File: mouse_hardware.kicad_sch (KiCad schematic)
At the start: 48 parts, among them IC1 ADP150AUJZ-2.0-R7, IC2 AP2112K-3.3TRG1, J1 Conn_01x04_Pin, J2 Conn_01x04_Pin, SW1 SW_Push, SW5 SW_Push, U1 STM32F103RETx, U2 PMW3360DM-T2QU, Y1 8MHz

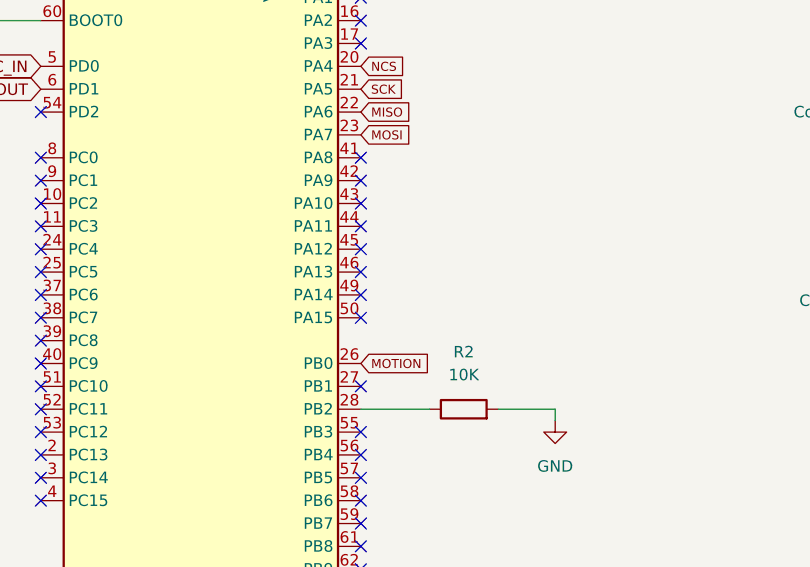
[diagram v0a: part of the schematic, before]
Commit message: Connect SCLK and SWDIO
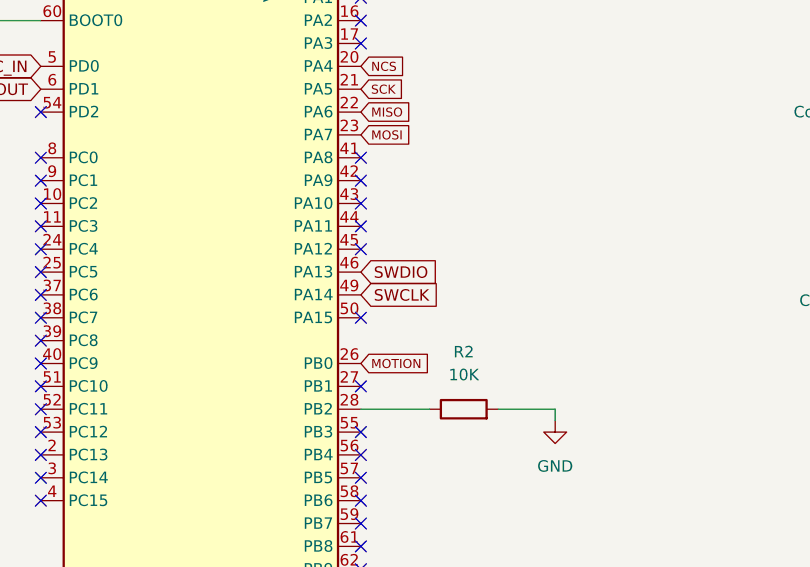
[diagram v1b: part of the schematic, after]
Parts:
- H1, H2, H3: footprint (none) -> Hole:Hole_1.8mm_1.2mm
- J1, J2: footprint Connector_PinHeader_2.54mm:PinHeader_1x04_P2.54mm_Horizontal -> PinHeader:PinHeader_1x04_P2.54mm_Horizontal
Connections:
- net SWCLK: now also U1.49 (PA14)
- net SWDIO: now also U1.46 (PA13)
- no-connect marks 41 -> 39
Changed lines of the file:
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@@
   (no_connect (at 227.33 127))
   (no_connect (at 227.33 200.66))
-  (no_connect (at 227.33 160.02))
   (no_connect (at 227.33 205.74))
   (no_connect (at 227.33 175.26))
@@
   (no_connect (at 191.77 147.32))
   (no_connect (at 80.01 54.61))
-  (no_connect (at 227.33 157.48))
   (no_connect (at 227.33 177.8))
   (no_connect (at 191.77 182.88))
@@
     )
   )
+  (global_label "SWCLK" (shape input) (at 227.33 160.02 0) (fields_autoplaced)
+    (effects (font (size 1.27 1.27)) (justify left))
+    (property "Intersheetrefs" "${INTERSHEET_REFS}" (at 236.5442 160.02 0)
+      (effects (font (size 1.27 1.27)) (justify left) hide)
+    )
+  )
   (global_label "USBDP" (shape input) (at 228.6 198.12 0) (fields_autoplaced)
     (effects (font (size 1 1)) (justify left))
@@
     )
   )
+  (global_label "SWDIO" (shape input) (at 227.33 157.48 0) (fields_autoplaced)
+    (effects (font (size 1.27 1.27)) (justify left))
+    (property "Intersheetrefs" "${INTERSHEET_REFS}" (at 236.1814 157.48 0)
+      (effects (font (size 1.27 1.27)) (justify left) hide)
+    )
+  )
   (global_label "OSC_OUT" (shape input) (at 191.77 137.16 180) (fields_autoplaced)
     (effects (font (size 1.27 1.27)) (justify right))
@@
       (effects (font (size 1.27 1.27)) (justify left))
     )
-    (property "Footprint" "" (at 44.45 180.34 0)
+    (property "Footprint" "Hole:Hole_1.8mm_1.2mm" (at 44.45 180.34 0)
       (effects (font (size 1.27 1.27)) hide)
     )
@@
       (effects (font (size 1.27 1.27)) (justify left))
     )
-    (property "Footprint" "" (at 41.91 214.63 0)
+    (property "Footprint" "Hole:Hole_1.8mm_1.2mm" (at 41.91 214.63 0)
       (effects (font (size 1.27 1.27)) hide)
     )
@@
       (effects (font (size 1.27 1.27)) (justify left))
     )
-    (property "Footprint" "" (at 41.275 251.46 0)
+    (property "Footprint" "Hole:Hole_1.8mm_1.2mm" (at 41.275 251.46 0)
       (effects (font (size 1.27 1.27)) hide)
     )
@@
       (effects (font (size 1.27 1.27)))
     )
-    (property "Footprint" "Connector_PinHeader_2.54mm:PinHeader_1x04_P2.54mm_Horizontal" (at 282.575 165.735 0)
+    (property "Footprint" "PinHeader:PinHeader_1x04_P2.54mm_Horizontal" (at 282.575 165.735 0)
       (effects (font (size 1.27 1.27)) hide)
     )
@@
       (effects (font (size 1.27 1.27)))
     )
-    (property "Footprint" "Connector_PinHeader_2.54mm:PinHeader_1x04_P2.54mm_Horizontal" (at 281.94 144.78 0)
-      (effects (font (size 1.27 1.27)) hide)
-    )
+    (property "Footprint" "PinHeader:PinHeader_1x04_P2.54mm_Horizontal" (at 281.94 144.78 0)
+      (effects (font (size 1.27 1.27)) hide)
+    )

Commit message: rev3
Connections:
- net USBDM: now also U1.44 (PA11); no longer U1.30 (PB11)
- net USBDP: now also U1.45 (PA12); no longer U1.33 (PB12)
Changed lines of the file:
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@@
   (no_connect (at 227.33 205.74))
   (no_connect (at 227.33 175.26))
+  (no_connect (at 227.33 198.12))
   (no_connect (at 191.77 167.64))
   (no_connect (at 191.77 177.8))
@@
   (no_connect (at 191.77 182.88))
   (no_connect (at 227.33 162.56))
-  (no_connect (at 227.33 154.94))
   (no_connect (at 191.77 160.02))
+  (no_connect (at 227.33 195.58))
   (no_connect (at 227.33 187.96))
   (no_connect (at 227.33 132.08))
@@
   (no_connect (at 191.77 157.48))
   (no_connect (at 191.77 152.4))
-  (no_connect (at 227.33 152.4))
   (no_connect (at 191.77 172.72))
   (no_connect (at 227.33 129.54))
@@
     (stroke (width 0) (type default))
   )
-  (wire (pts (xy 227.33 198.12) (xy 228.6 198.12))
-    (stroke (width 0) (type default))
-  )
   (wire (pts (xy 121.92 53.34) (xy 124.46 53.34))
     (stroke (width 0) (type default))
@@
   )
   (wire (pts (xy 82.55 30.48) (xy 87.63 30.48))
-    (stroke (width 0) (type default))
-  )
-  (wire (pts (xy 227.33 195.58) (xy 228.6 195.58))
     (stroke (width 0) (type default))
   )
@@
     )
   )
-  (global_label "USBDP" (shape input) (at 228.6 198.12 0) (fields_autoplaced)
+  (global_label "USBDP" (shape input) (at 227.33 154.94 0) (fields_autoplaced)
     (effects (font (size 1 1)) (justify left))
-    (property "Intersheetrefs" "${INTERSHEET_REFS}" (at 235.9503 198.12 0)
+    (property "Intersheetrefs" "${INTERSHEET_REFS}" (at 234.6803 154.94 0)
       (effects (font (size 1.27 1.27)) (justify left) hide)
     )
@@
     )
   )
-  (global_label "USBDM" (shape input) (at 228.6 195.58 0) (fields_autoplaced)
+  (global_label "USBDM" (shape input) (at 227.33 152.4 0) (fields_autoplaced)
     (effects (font (size 1 1)) (justify left))
-    (property "Intersheetrefs" "${INTERSHEET_REFS}" (at 236.0932 195.58 0)
-      (effects (font (size 1.27 1.27)) (justify left) hide)
-    )
+    (property "Intersheetrefs" "${INTERSHEET_REFS}" (at 234.8232 152.4 0)
+      (effects (font (size 1.27 1.27)) (justify left) hide)
+    )
